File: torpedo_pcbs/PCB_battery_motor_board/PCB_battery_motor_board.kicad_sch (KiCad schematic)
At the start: 30 parts, among them IC1 BQ25672RQMR, IC4 TCM680EOA, J1 B2B-XH-A, J2 S5B-PH-K-S_LF__SN_, J3 B2B-XH-A (actually ph), J4 B2B-XH-A (actually ph), J5 B2B-XH-A, J6 B2B-XH-A, J7 505110-0492, U1 AMS1117-3.3

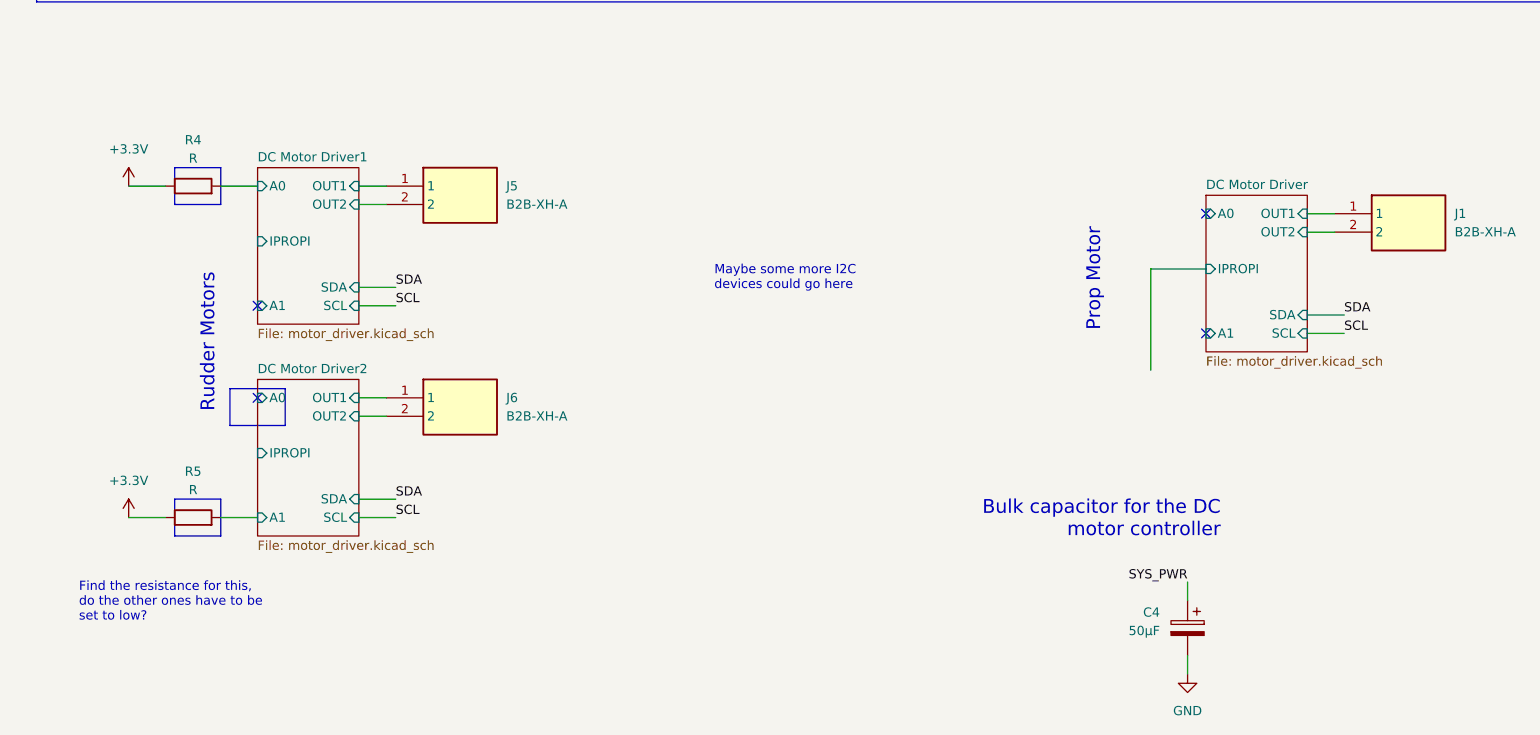
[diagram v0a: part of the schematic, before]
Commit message: psram already in esp32, minor updates
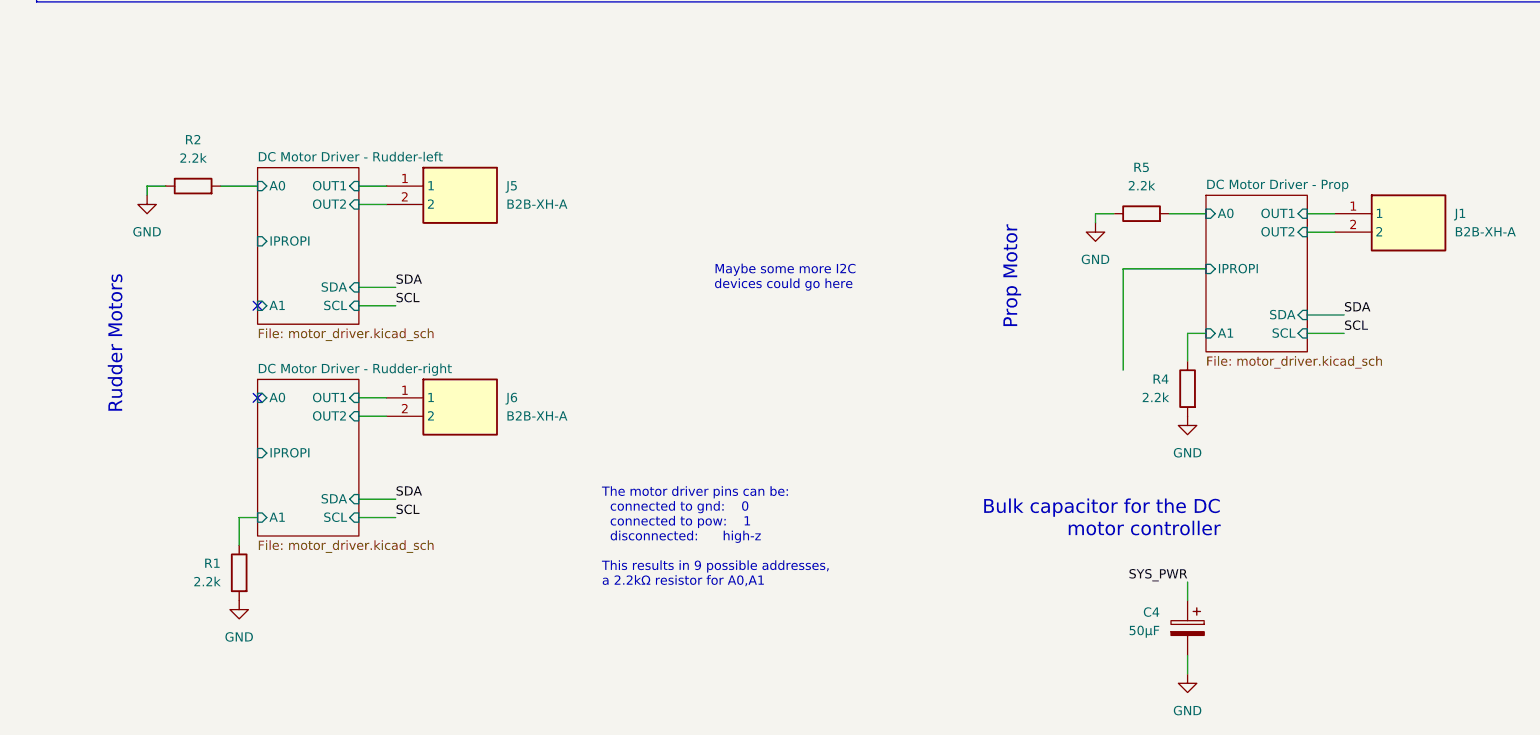
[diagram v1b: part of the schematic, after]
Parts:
- added R1, R2: 2.2k, symbol Device:R
- R4, R5: value R -> 2.2k
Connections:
- net +3.3V: no longer R4.1, R5.1
- net DC Motor Driver - Prop/A0: now also R5.2
- net DC Motor Driver - Prop/A1: now also R4.1
- net DC Motor Driver - Rudder-left/A0: now also R2.2; no longer R4.2
- net DC Motor Driver - Rudder-right/A1: now also R1.1; no longer R5.2
- net GND: now also R4.2, R5.1, R1.2, R2.1
- no-connect marks 11 -> 9
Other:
- sheet DC Motor Driver renamed DC Motor Driver - Prop
- sheet DC Motor Driver1 renamed DC Motor Driver - Rudder-left
- sheet DC Motor Driver2 renamed DC Motor Driver - Rudder-right
- note added: "The motor driver pins can be: connected to gnd: 0 connected to pow: 1 disconnected: high-z This results in 9 possible addresses, a 2.2kΩ resistor for A0,A1"
- note removed: "Find the resistance for this, do the other ones have to be set to low?"

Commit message: daugther board started
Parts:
- removed 4.7μF, 4.7μF1: C_Polarized, symbol Device:C_Polarized
- removed C17, C18, C19: 47nF, symbol Device:C
- removed C20, C21: 4.7μF, symbol Device:C
- removed C7: 1nF, symbol Device:C
- removed D1: LED, symbol Device:LED
- removed IC1: BQ25672RQMR, BQ25672RQMR, symbol SamacSys_Parts:BQ25672RQMR
- removed IC4: TCM680EOA, SOIC127P600X175-8N, symbol SamacSys_Parts:TCM680EOA
- removed J1, J5, J6: B2B-XH-A, SHDR2W64P0X250_1X2_740X575X700P, symbol SamacSys_Parts:B2B-XH-A
- removed J2: S5B-PH-K-S_LF__SN_, S5BPHKSLFSN, symbol SamacSys_Parts:S5B-PH-K-S_LF__SN_
- removed J3, J4: B2B-XH-A (actually ph), SHDR2W64P0X250_1X2_740X575X700P, symbol SamacSys_Parts:B2B-XH-A
- removed J7: 505110-0492, 5051100492, symbol SamacSys_Parts:505110-0492
- removed L1: 1μH, symbol Device:L
- removed R19, R4, R5: 2.2k, symbol Device:R
- removed R20: 100, symbol Device:R
- removed TH1: 103AT-2 10k, symbol Device:Thermistor_NTC
- added C10: 47nF, Capacitor_SMD:C_0805_2012Metric_Pad1.18x1.45mm_HandSolder, symbol Device:C
- added C11, C5: 10μF, Capacitor_SMD:C_0805_2012Metric_Pad1.18x1.45mm_HandSolder, symbol Device:C
- added C13: 4.7μF, Capacitor_SMD:C_0805_2012Metric_Pad1.18x1.45mm_HandSolder, symbol Device:C
- added D2, D3: LED, LED_SMD:LED_0805_2012Metric, symbol Device:LED
- added IC2: BQ25601RTWR, SamacSys_Parts:QFN50P400X400X80-25N-D, symbol SamacSys_Parts:BQ25601RTWR
- added J1, J4: Conn_01x01, Connector_PinSocket_2.00mm:PinSocket_1x01_P2.00mm_Vertical, symbol Connector_Generic:Conn_01x01
- added J10: Conn_01x05, Connector_PinSocket_2.00mm:PinSocket_1x05_P2.00mm_Vertical, symbol Connector_Generic:Conn_01x05
- added J3, J5, J6, J8, J9: Conn_01x02, Connector_PinSocket_2.00mm:PinSocket_1x02_P2.00mm_Vertical, symbol Connector_Generic:Conn_01x02
- added J7: Conn_01x04, Connector_PinSocket_2.00mm:PinSocket_1x04_P2.00mm_Vertical, symbol Connector_Generic:Conn_01x04
- added L2: 1μH, Inductor_SMD:L_0805_2012Metric_Pad1.05x1.20mm_HandSolder, symbol Device:L
- added R10, R11, R12, R13: 10k, Resistor_SMD:R_0805_2012Metric_Pad1.20x1.40mm_HandSolder, symbol Device:R
- added R3, R9: 2.2k, Resistor_SMD:R_0805_2012Metric_Pad1.20x1.40mm_HandSolder, symbol Device:R
- added R8: 0??, Resistor_SMD:R_0805_2012Metric_Pad1.20x1.40mm_HandSolder, symbol Device:R
- C1, C2, C4: footprint (none) -> Capacitor_SMD:C_0805_2012Metric_Pad1.18x1.45mm_HandSolder
- R1, R2, R7: footprint (none) -> Resistor_SMD:R_0805_2012Metric_Pad1.20x1.40mm_HandSolder
- R6: value 8.2k -> 10k; footprint (none) -> Resistor_SMD:R_0805_2012Metric_Pad1.20x1.40mm_HandSolder
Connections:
- net PROG is gone; now on net +3.3V: R6.1
- net +3.3V: now also J10.1 (Pin_1), J7.4 (Pin_4)
- net DC Motor Driver - Prop/A0: now also R3.2
- net DC Motor Driver - Prop/A1: now also R9.1
- net DC Motor Driver - Prop/OUT1: now also J3.1 (Pin_1)
- net DC Motor Driver - Prop/OUT2: now also J3.2 (Pin_2)
- net DC Motor Driver - Rudder-left/OUT1: now also J6.1 (Pin_1)
- net DC Motor Driver - Rudder-left/OUT2: now also J6.2 (Pin_2)
- net DC Motor Driver - Rudder-right/OUT1: now also J8.1 (Pin_1)
- net DC Motor Driver - Rudder-right/OUT2: now also J8.2 (Pin_2)
- net GND: now also C11.1, C13.2, C5.2, IC2.17 (GND_1), IC2.18 (GND_2), IC2.2 (PSEL), IC2.25 (THERMAL_PAD), IC2.9 (~{CE}), J10.3 (Pin_3), J7.3 (Pin_3), J9.2 (Pin_2), R11.2, R13.1, R3.1, R9.2; no longer R6.2
- net REGN: now also C13.1, IC2.22 (REGN), R10.2
- net SCL: now also IC2.5 (SCL), J10.4 (Pin_4), J7.1 (Pin_1)
- net SDA: now also IC2.6 (SDA), J10.5 (Pin_5), J7.2 (Pin_2)
- net SYS_PWR: now also C5.1, D2.2 (A), D3.2 (A), IC2.15 (SYS_1), IC2.16 (SYS_2), L2.2
- net VBUS: now also IC2.1 (VAC), IC2.24 (VBUS), J10.2 (Pin_2)
- net VREF: now reaches R7.1
- net VREF: now also R6.2
- new net: IC2.21 (BTST), R8.1
- new net: C10.1, R8.2
- new net: IC2.7 (~{INT}), J1.1 (Pin_1)
- new net: IC2.11 (TS), R10.1, R11.1
- new net: IC2.13 (BAT_1), IC2.14 (BAT_2), J9.1 (Pin_1), R12.2
- new net: C10.2, IC2.19 (SW_1), IC2.20 (SW_2), L2.1
- new net: C11.2, IC2.23 (PMID)
- new net: D2.1 (K), IC2.3 (~{PG})
- new net: D3.1 (K), IC2.4 (STAT)
- new net: J4.1 (Pin_1), R12.1, R13.2
- new net DC Motor Driver - Extra/OUT1: J5.1 (Pin_1)
- new net DC Motor Driver - Extra/OUT2: J5.2 (Pin_2)
- no-connect marks 9 -> 7
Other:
- added sheet DC Motor Driver - Extra (motor_driver.kicad_sch)
- sheet DC Motor Driver - Prop ports: added none; removed IPROPI
- sheet DC Motor Driver - Rudder-left ports: added none; removed IPROPI
- sheet DC Motor Driver - Rudder-right ports: added none; removed IPROPI
- note added: "I2C connector for future use"
- note added: "OPEN Qs: Is 2.4 current cutoff ok? Can charging always be enabled? Should I have a thermistor?"
- note added: "PSEL driven low => 2.4A current limit"
- note removed: "Connecting this to REGN will set the max allowing me to control it via I2C"
- note removed: "I2C connector for flexi-PCB with pressure sensors"
- note removed: "Make sure that you can just <----- ignore USB like this on the D+/D- pins Also it looks like VBUS needs to be 9-20V, so I might have to step the USB power up (FIXED) I changed the label for the thermistor to the reccommended one. You'll still have to find the footprint. Or maybe just ignore it and let the lipos explode. CH340C is connected to VBUS, should it be connected to the batt manager inste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"
- note removed: "Prop Motor"
- note removed: "Questions for an electrical person: - Why would you need multiple decoupling capacitors of the same capacitors for a pin? Am I misunderstanding what they want?"
- note removed: "Rudder Motors"
- note removed: "TBD: Voltage divider"
- note removed: "This programs the a 2s cell count with a switching freq of 750 kHz, I chose the switching freq mostly blind"
- note removed: "Verify that this matches the polarity of the motor connection"
- moved on the sheet: C1, C2, R1, R2, U1

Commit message: daughter board updates
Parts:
- added R19, R20, R4, R5: 0, Resistor_SMD:R_0805_2012Metric_Pad1.20x1.40mm_HandSolder, symbol Device:R
- J10: footprint Connector_PinSocket_2.00mm:PinSocket_1x05_P2.00mm_Vertical -> SamacSys_Parts:S5BPHKSLFSN
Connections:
- net SDA: now also R19.2, R20.2, R4.2, R5.2
- new net DC Motor Driver - Extra/SDA: R20.1
- new net DC Motor Driver - Prop/SDA: R19.1
- new net DC Motor Driver - Rudder-left/SDA: R4.1
- new net DC Motor Driver - Rudder-right/SDA: R5.1
